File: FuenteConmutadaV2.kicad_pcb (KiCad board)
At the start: 2 copper layers, 75.7 x 39.9 mm, 23 parts, among them J1 Conn_01x01_Pin, J2 Conn_01x01_Pin, J4 Conn_01x01_Pin, J5 USB_C_Receptacle_USB2.0

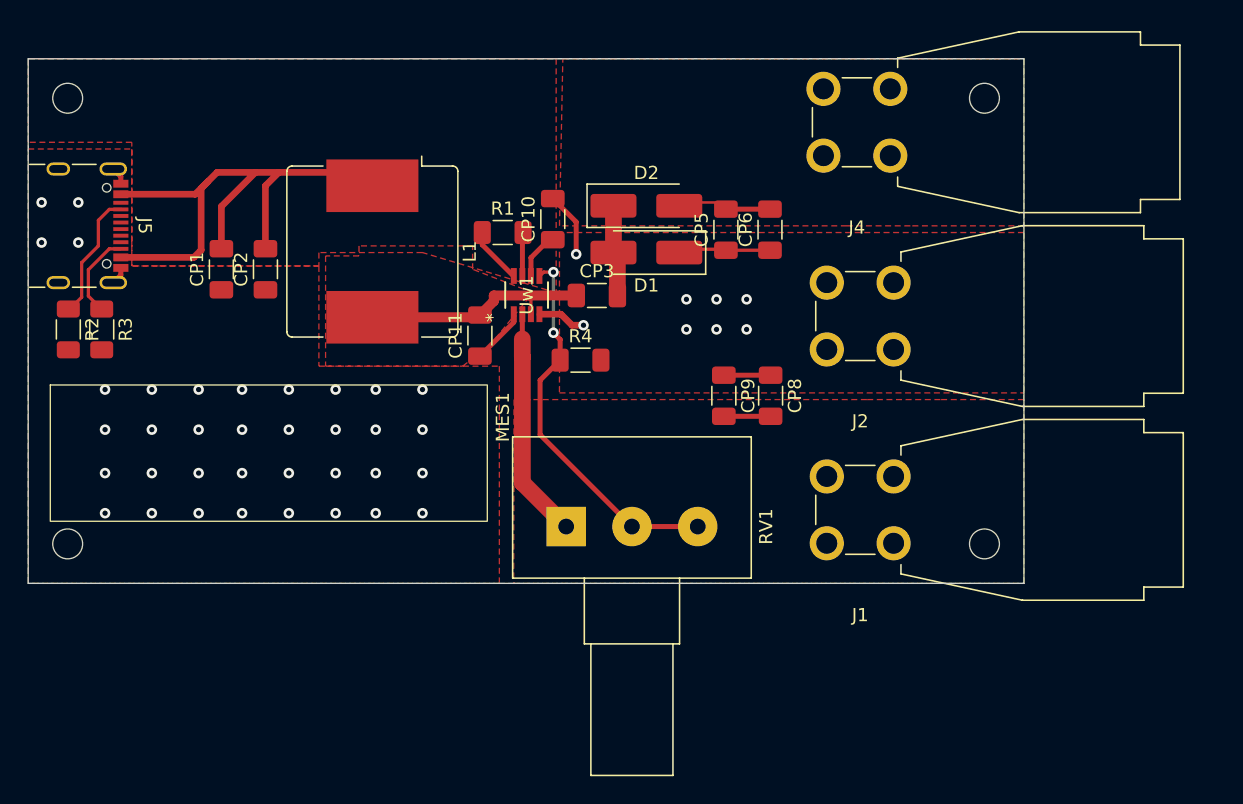
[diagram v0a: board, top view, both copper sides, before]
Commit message: LED indicador y Resistencias de carga
Se agrego un LED rojo indicador de que se encuentra alimentada la placa, junto a resistencias con agujeros pasantes para las cargas.
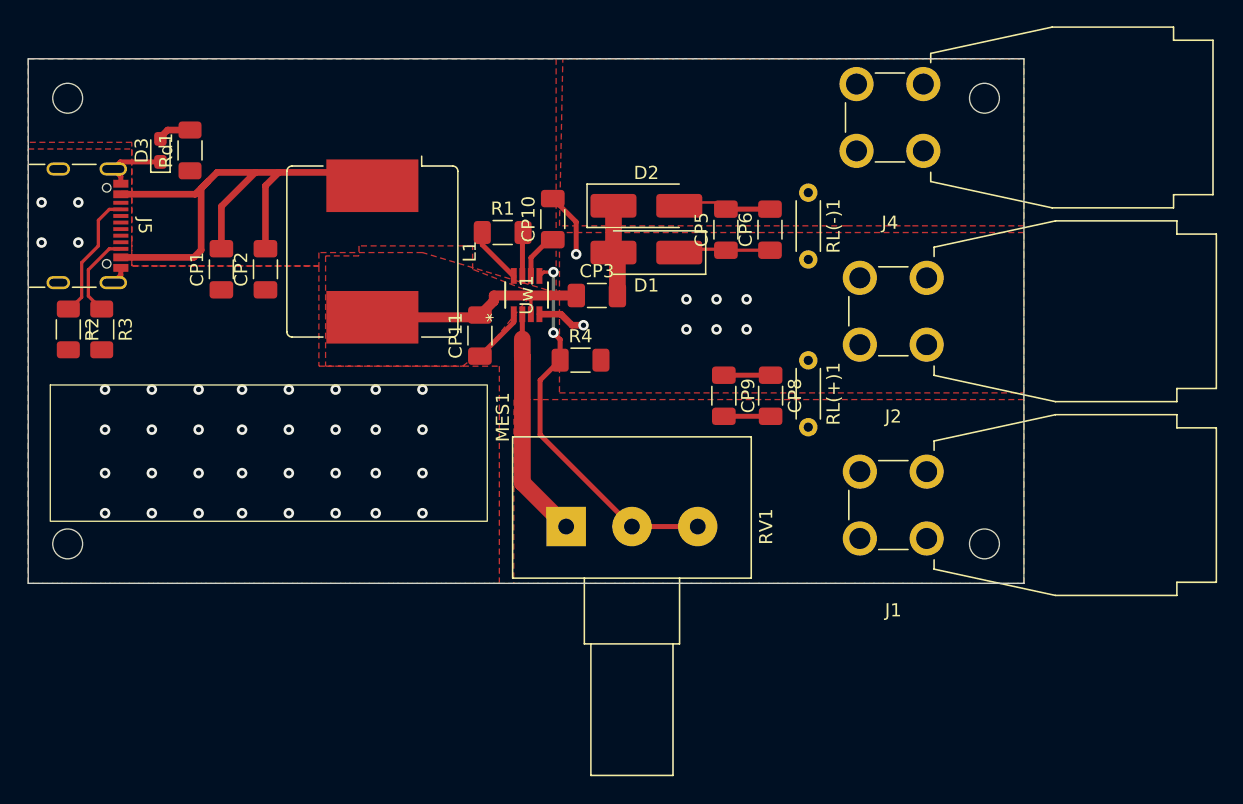
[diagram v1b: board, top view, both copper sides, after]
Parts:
- added D3: LED Red, LED_SMD:LED_0603_1608Metric_Pad1.05x0.95mm_HandSolder, F.Cu at (118.0, 88.5)
- added RL(+)1: 470, Resistor_THT:R_Axial_DIN0204_L3.6mm_D1.6mm_P5.08mm_Horizontal, F.Cu at (167.2, 104.5)
- added RL(-)1: 470, Resistor_THT:R_Axial_DIN0204_L3.6mm_D1.6mm_P5.08mm_Horizontal, F.Cu at (167.2, 91.7)
- added Rd1: 220, Resistor_SMD:R_1206_3216Metric_Pad1.30x1.75mm_HandSolder, F.Cu at (120.2, 88.5)
- moved J1 2.54 mm to (176.2, 118.0)
- moved J2 2.54 mm to (176.2, 103.3)
- moved J4 2.54 mm to (176.0, 88.5)
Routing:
- net GND: track 21.8 -> 25.6 mm
- net Net-(D3-A): track 0.00 -> 2.60 mm

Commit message: Led-Huecos voltimetro y esquinas  -R paralelo
-Cambie huella de LED a 1206 y posicione junto al display.
-Agregue agujeros (3mm) para fijar el voltímetro .
- Agregue R paralelo al potenciómetro.
-cambie Huecos de las esquinas a 3mm y un margen de 5 mm (Diametro)
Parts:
- added RP1: R, Resistor_SMD:R_1206_3216Metric_Pad1.30x1.75mm_HandSolder, F.Cu at (150.0, 108.5)
- D3: footprint LED_SMD:LED_0603_1608Metric_Pad1.05x0.95mm_HandSolder -> LED_SMD:LED_1206_3216Metric
- moved D3 14.0 mm to (120.8, 102.2), turned to -90 degrees
- moved Rd1 13.8 mm to (118.0, 102.1), turned to -90 degrees
- moved MES1 0.21 mm to (124.8, 111.5)
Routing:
- net +5V: track 49.4 -> 54.5 mm
- net GND: track 25.6 -> 22.8 mm
- net Net-(Uw1-FB): track 29.3 -> 31.3 mm
- net Net-(D3-A): track 2.60 -> 3.26 mm
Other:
- outline, holes or cut-outs redrawn

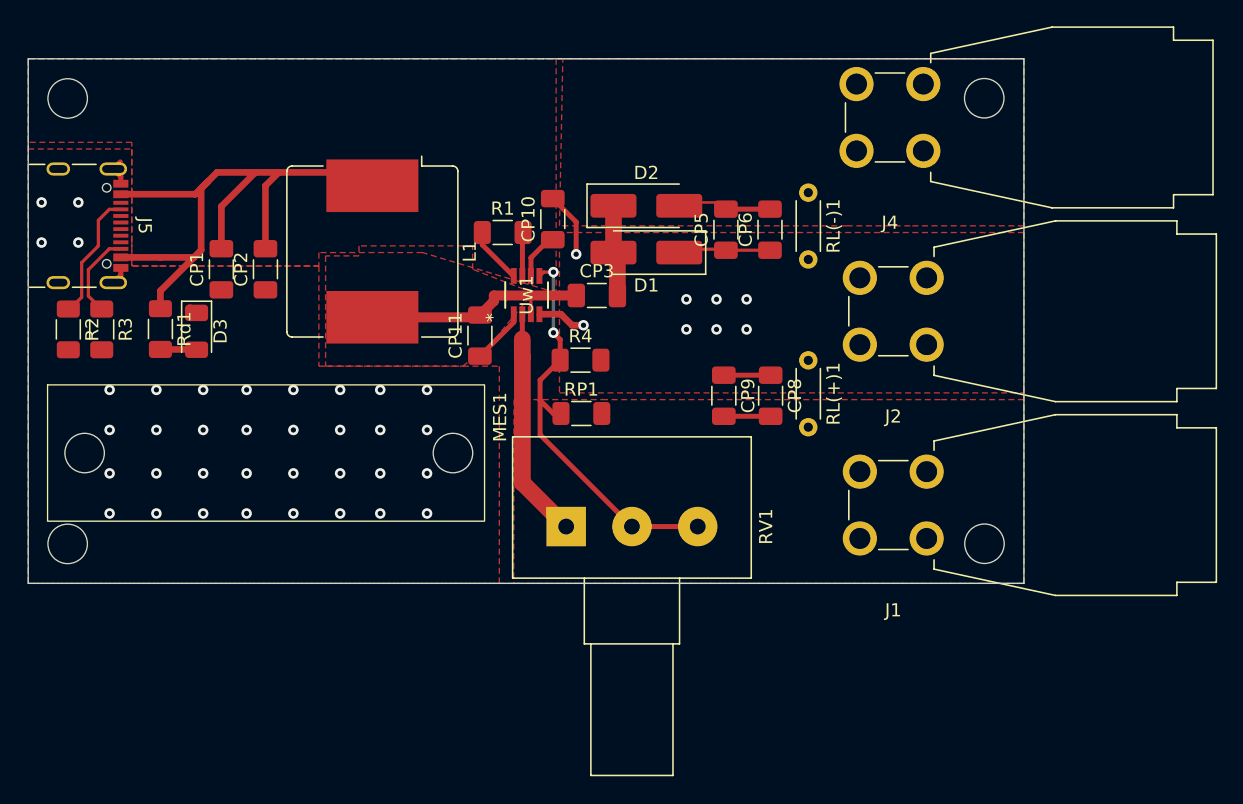
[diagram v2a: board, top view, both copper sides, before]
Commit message: Cambios+pad banana
Pad banana diseñado
ajuste te tamaño de placa 80x40mm
ajuste vias
+mounting holes
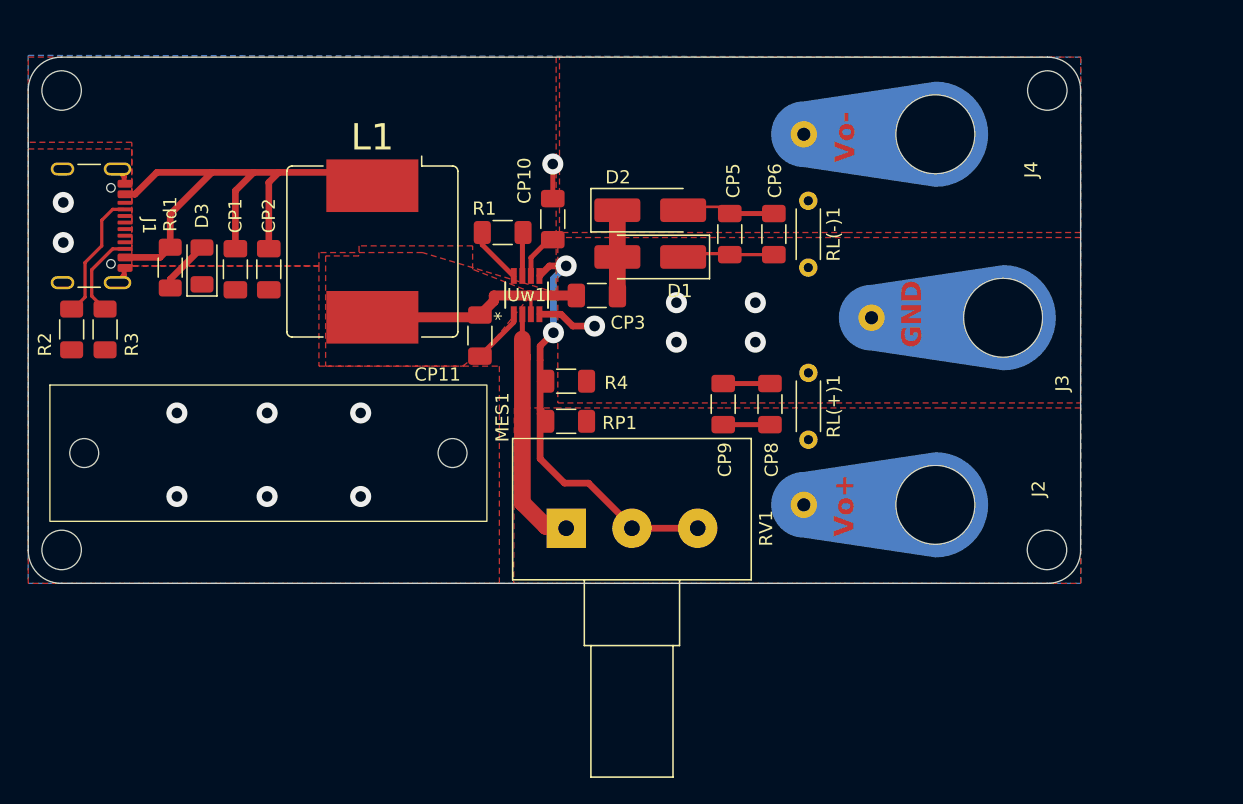
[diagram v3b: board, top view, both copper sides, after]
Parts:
- removed J5: USB_C_Receptacle_USB2.0, Connector_USB:USB_C_Receptacle_GCT_USB4105-xx-A_16P_TopMnt_Horizontal
- added J3: Conn_01x01_Pin, Banana_elemon:Banana_209_elemon, F.Cu at (182.1, 101.2)
- added REF**: MountingHole 3mm, Agujero3mm:MountingHole 3mm, F.Cu at (110.5, 118.9)
- added REF**: MountingHole 3mm, Agujero3mm:MountingHole 3mm, F.Cu at (110.5, 83.9)
- added REF**: MountingHole 3mm, Agujero3mm:MountingHole 3mm, F.Cu at (185.4, 83.9)
- added REF**: MountingHole 3mm, Agujero3mm:MountingHole 3mm, F.Cu at (185.4, 118.9)
- J1: value Conn_01x01_Pin -> USB_C_Receptacle_USB2.0; footprint Connector:CalTest_CT3151 -> Connector_USB:USB_C_Receptacle_GCT_USB4105-xx-A_16P_TopMnt_Horizontal
- J2, J4: footprint Connector:CalTest_CT3151 -> Banana_elemon:Banana_209_elemon
- moved J1 68.8 mm to (111.6, 94.2), turned to -90 degrees
- moved J2 12.2 mm to (176.9, 115.4)
- moved D3 4.98 mm to (121.2, 97.3), turned to 90 degrees
- moved Rd1 4.73 mm to (118.7, 97.4)
- moved R4 1.94 mm to (148.8, 106.0)
- moved J4 1.56 mm to (176.9, 87.3)
- moved MES1 1.46 mm to (126.2, 111.5)
- moved RP1 1.30 mm to (148.8, 109.1)
- moved CP1 1.06 mm to (123.7, 97.5)
- moved RL(+)1 0.95 mm to (167.3, 105.4)
- moved CP8 0.64 mm to (164.3, 107.8)
- moved CP9 0.64 mm to (160.8, 107.8)
- moved RL(-)1 0.62 mm to (167.2, 92.3)
- moved CP5 0.45 mm to (161.3, 94.9)
- moved CP6 0.45 mm to (164.6, 94.9)
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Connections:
- J2 pad 1: GND -> /Vo+
- R2 pad 1: Net-(J5-CC1) -> Net-(J1-CC1)
- R3 pad 1: Net-(J5-CC2) -> Net-(J1-CC2)
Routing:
- net Net-(J1-CC1): track 0.00 -> 9.81 mm
- net Net-(J5-CC1): track 9.81 -> 0.00 mm
- net +5V: track 54.5 -> 47.6 mm
- net Net-(J1-CC2): track 0.00 -> 6.55 mm
- net Net-(J5-CC2): track 6.55 -> 0.00 mm
- net GND: track 22.8 -> 20.4 mm, vias 44 -> 14
- net Net-(Uw1-FB): track 31.3 -> 32.2 mm
- net /Vo+: track 21.1 -> 22.0 mm
- net Net-(D3-A): track 3.26 -> 4.08 mm
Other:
- board size 75.7 x 39.9 mm -> 80 x 40 mm
- board text added: "GND"
- board text added: "Vo+"
- board text added: "Vo-"

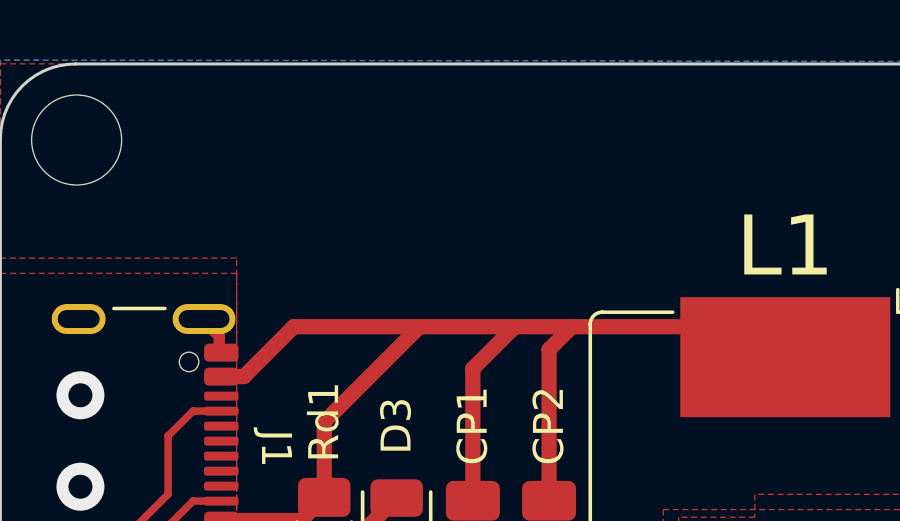
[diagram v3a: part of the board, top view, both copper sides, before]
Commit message: +pad 5V
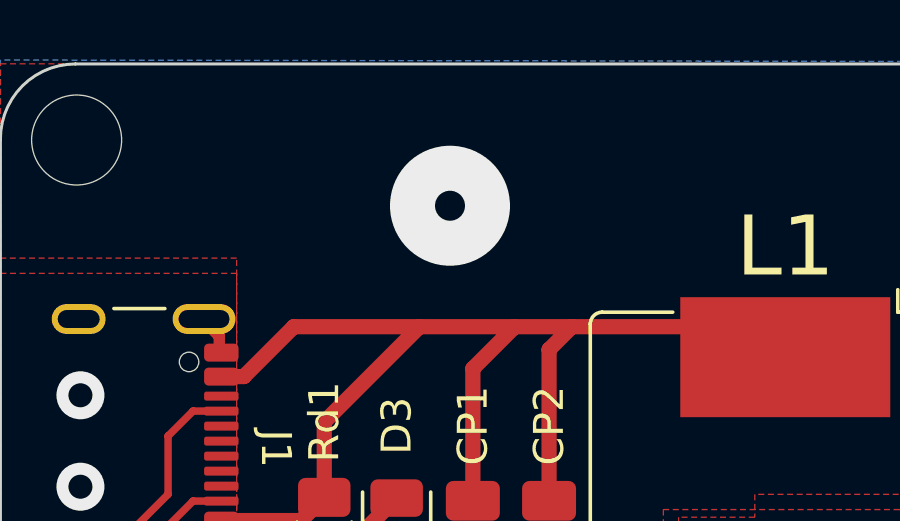
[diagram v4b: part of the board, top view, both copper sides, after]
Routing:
- net +5V: vias 0 -> 1

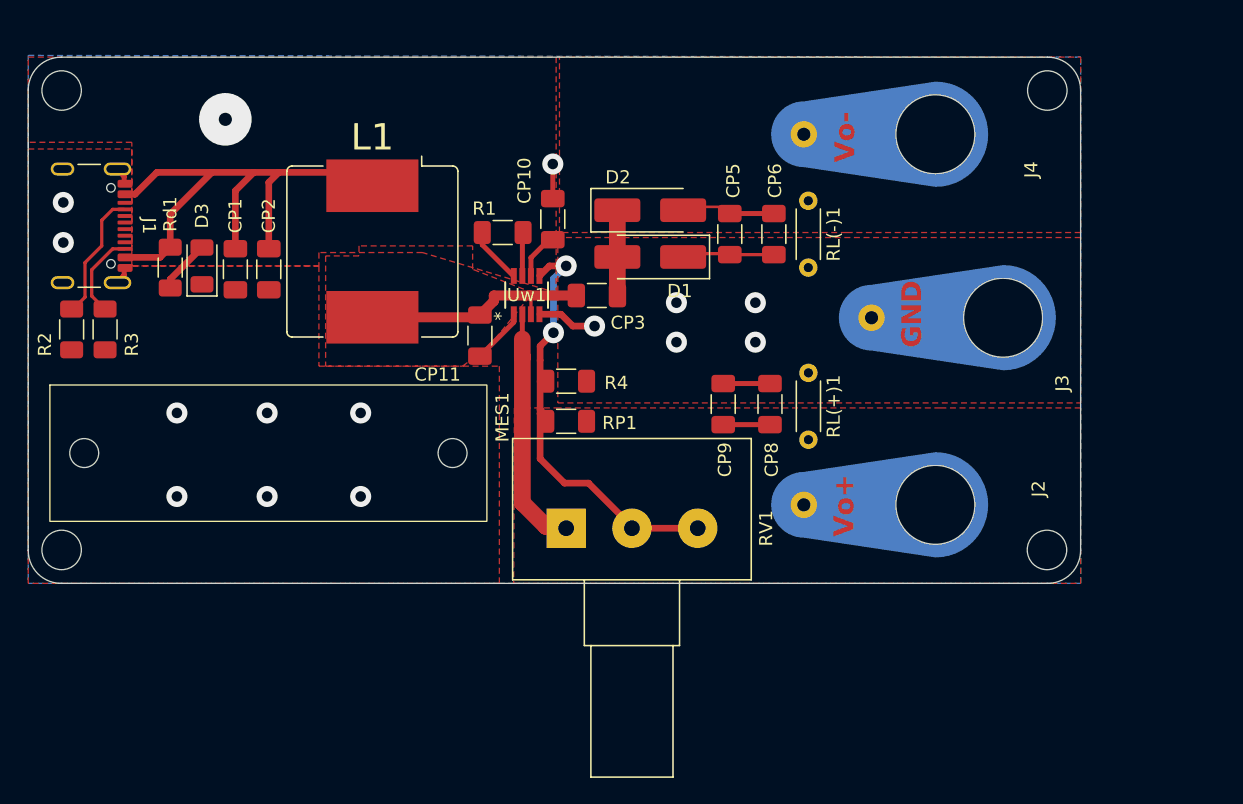
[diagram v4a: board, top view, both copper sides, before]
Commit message: Cambios
+pote
 +conectores banana
 +usb_c
+pads, footprints & 3dmodels
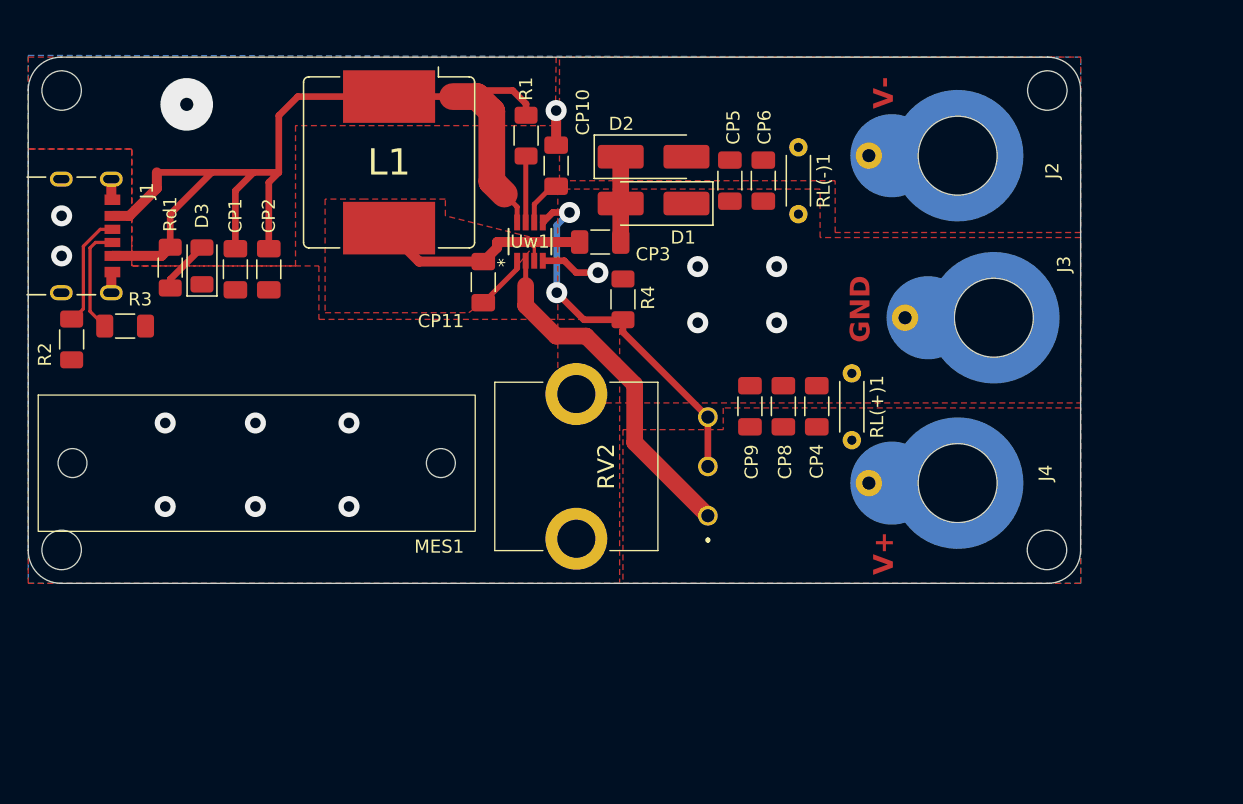
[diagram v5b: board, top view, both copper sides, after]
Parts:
- removed RP1: R, Resistor_SMD:R_1206_3216Metric_Pad1.30x1.75mm_HandSolder
- removed RV1: 100k, Potentiometer_THT:Potentiometer_Alps_RK163_Single_Horizontal
- added CP4: 22uF, Capacitor_SMD:C_1206_3216Metric_Pad1.33x1.80mm_HandSolder, F.Cu at (167.9, 108.0)
- added RV2: R_Potentiometer_MountingPin, Pote:PDB12M4251105BF, F.Cu at (159.6, 112.5)
- CP10: value 1uF -> 4.7uF
- CP11: value 1uF -> 0.1uF
- J1: footprint Connector_USB:USB_C_Receptacle_GCT_USB4105-xx-A_16P_TopMnt_Horizontal -> USB_Amphenol:AMPHENOL_10164359-00011LF
- J2, J3, J4: footprint Banana_elemon:Banana_209_elemon -> Banana_CT:Banana_CT_6mm
- moved J2 26.6 mm to (178.6, 88.9), turned to 0 degrees
- moved J4 26.6 mm to (178.6, 113.8), turned to 0 degrees
- moved R1 7.58 mm to (145.8, 87.4), turned to -90 degrees
- moved R4 7.57 mm to (153.2, 99.8), turned to 90 degrees
- moved L1 6.90 mm to (135.4, 89.4)
- moved CP6 4.14 mm to (163.8, 90.8)
- moved RL(-)1 4.13 mm to (166.5, 88.3)
- moved CP11 4.07 mm to (142.5, 98.5)
- moved Uw1 4.07 mm to (146.1, 95.4)
- moved CP10 4.07 mm to (148.1, 89.7)
- moved CP3 4.07 mm to (151.4, 95.5)
- moved D1 4.07 mm to (155.5, 92.5)
- moved D2 4.07 mm to (155.5, 89.0)
- moved CP5 4.06 mm to (161.3, 90.8)
- moved RL(+)1 3.30 mm to (170.6, 105.4)
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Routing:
- net +5V: track 47.6 -> 74.9 mm
- net GND: track 20.4 -> 10.7 mm
- net /Vo-: track 7.32 -> 1.80 mm
- net /Vo+: track 22.0 -> 26.5 mm
- net Net-(Uw1-FB): track 32.2 -> 28.5 mm
- net Net-(Uw1-EN): track 3.35 -> 5.09 mm
- net Net-(J1-CC2): track 6.55 -> 8.21 mm
- net Net-(J1-CC1): track 9.81 -> 8.71 mm
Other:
- board text added: "V+"
- board text added: "V-"
- board text removed: "Vo+"
- board text removed: "Vo-"

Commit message: Correccion footprint banana
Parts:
- R1: value R -> 30k
- R2, R3: value R -> 5k
- moved J2 24.9 mm to (178.6, 113.8)
- moved J4 24.9 mm to (178.6, 88.9)
